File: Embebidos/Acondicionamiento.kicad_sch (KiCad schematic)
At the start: 20 parts, among them IC1 ESP32-WROVER-B__8MB_, SW1 SW_Reset, SW2 SW_Boot

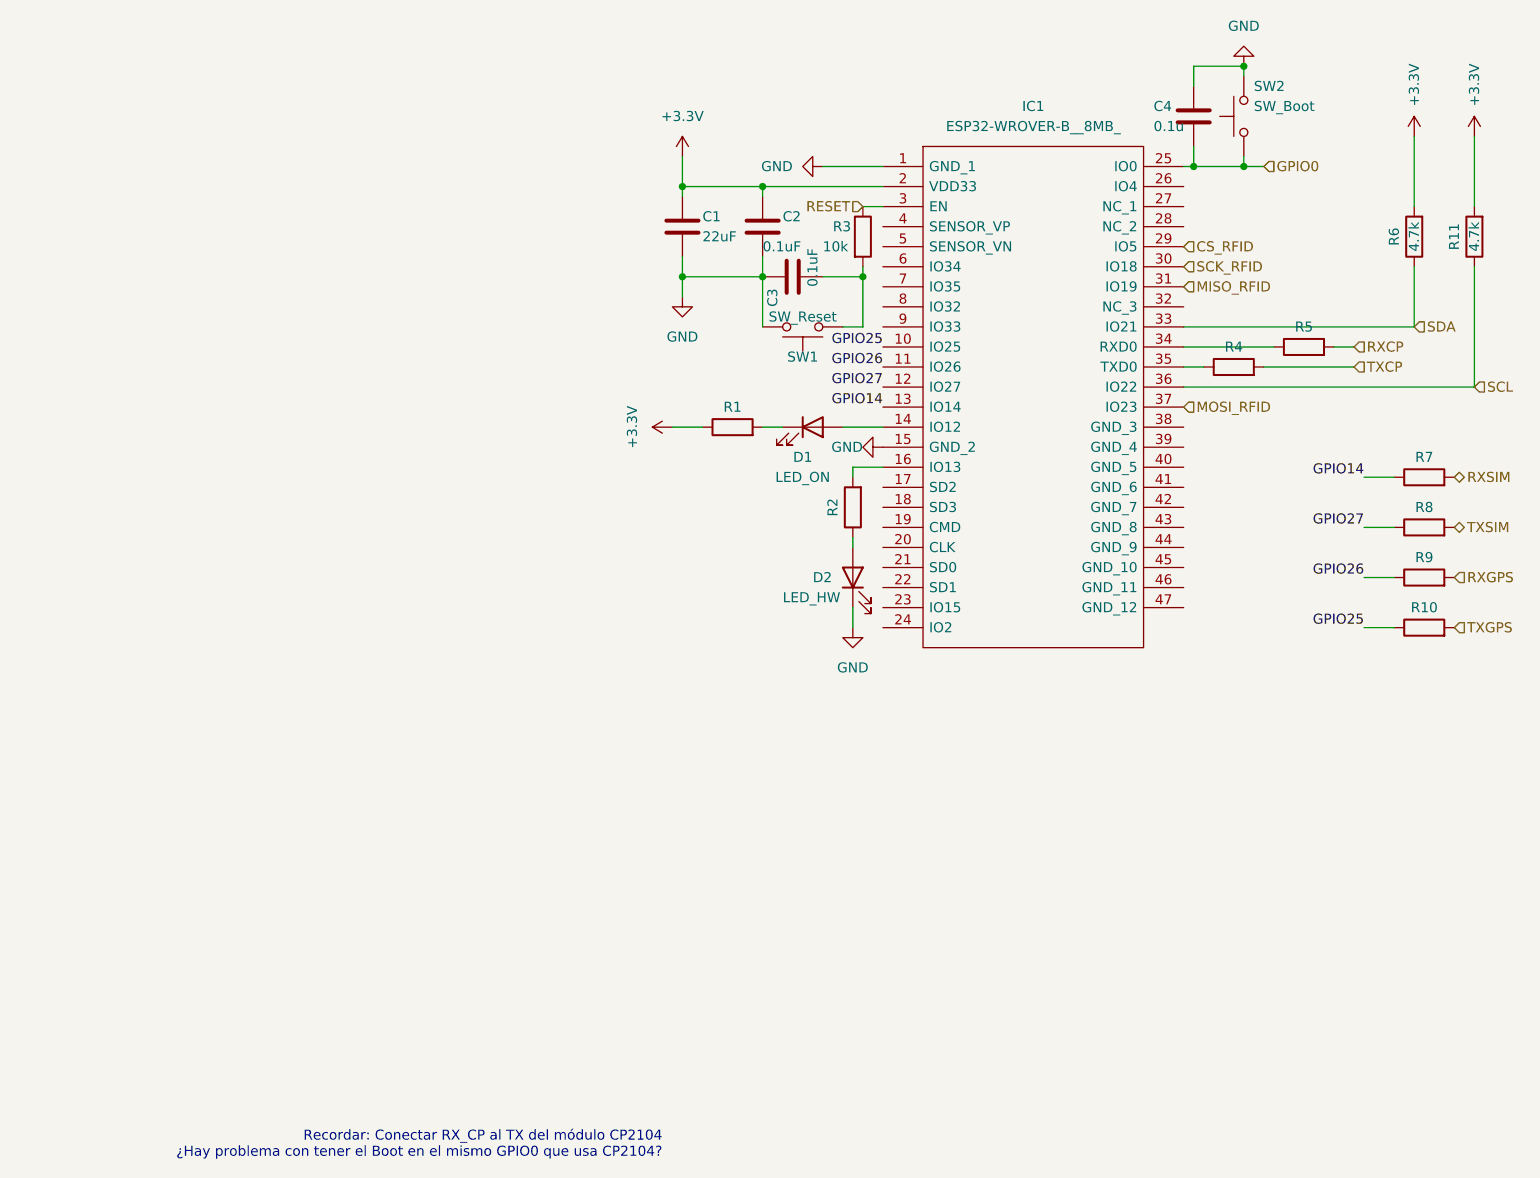
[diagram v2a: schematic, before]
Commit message: Luces delanteras, traseras, pantalla, e infrarrojo
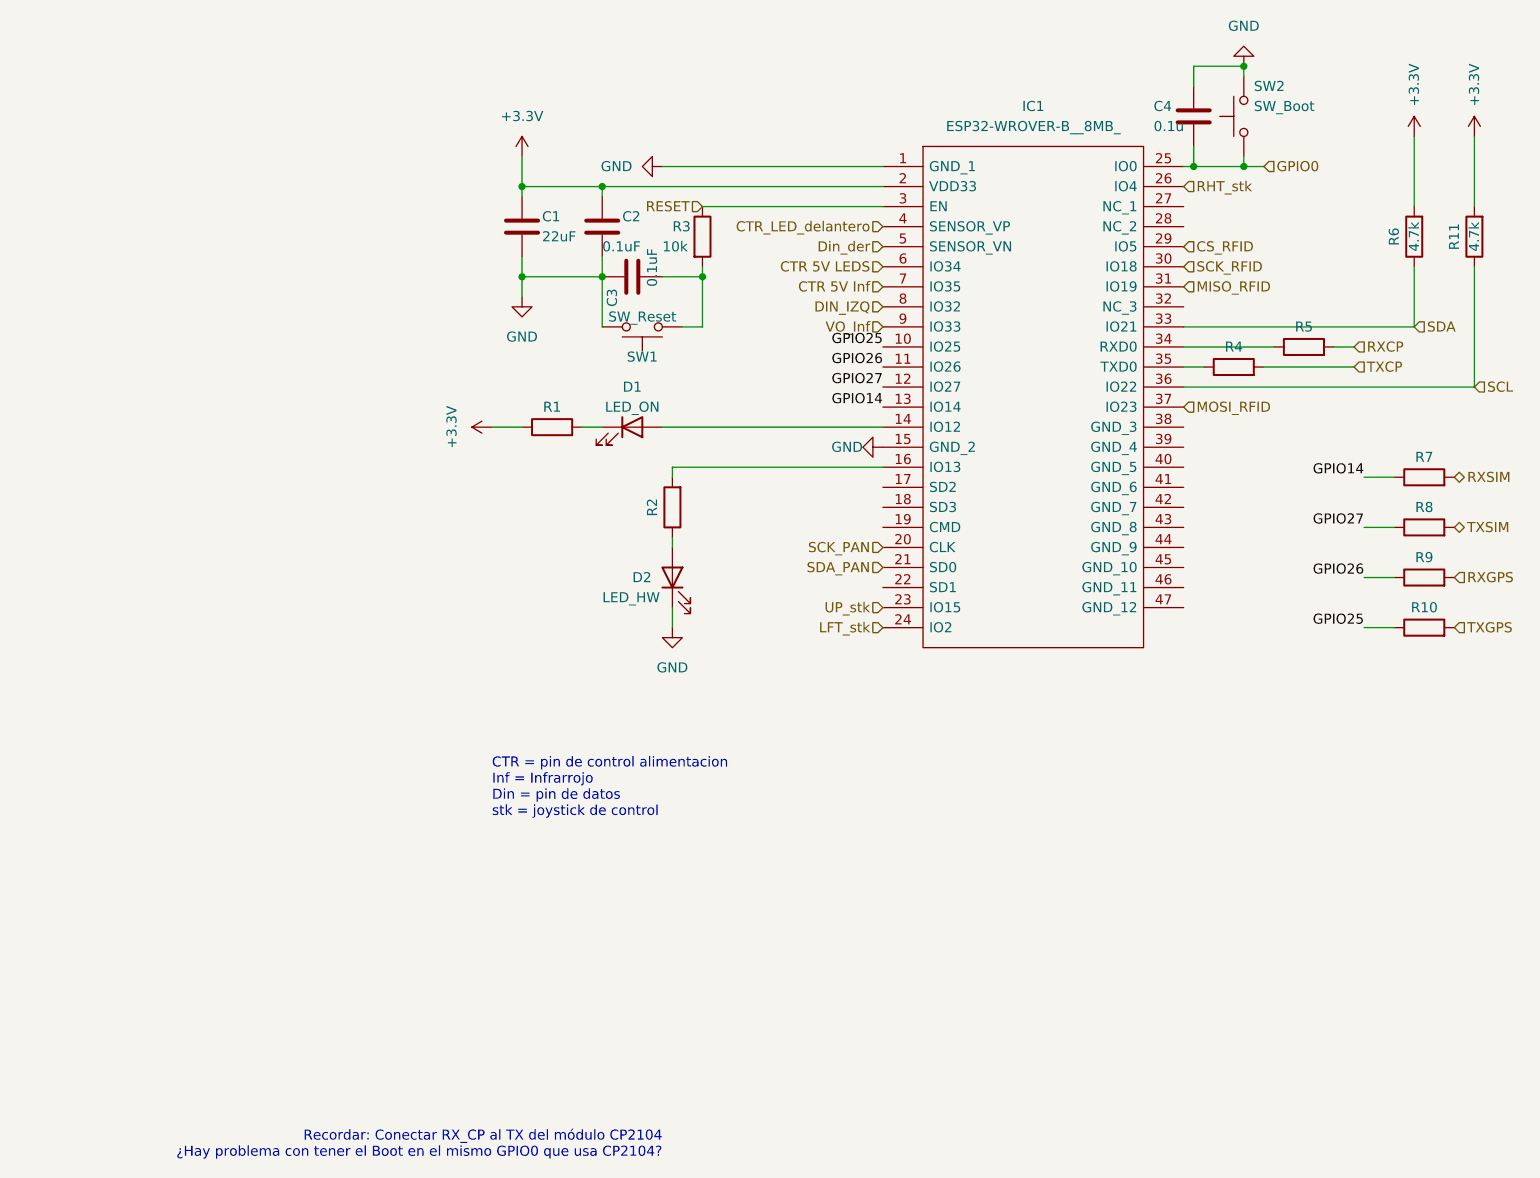
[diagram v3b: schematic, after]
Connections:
- net SCK_PAN: now reaches IC1.20 (CLK)
- net SDA_PAN: now reaches IC1.21 (SD0)
- net UP_stk: now reaches IC1.23 (IO15)
- net LFT_stk: now reaches IC1.24 (IO2)
- net RHT_stk: now reaches IC1.26 (IO4)
- net CTR_LED_delantero: now reaches IC1.4 (SENSOR_VP)
- net Din_der: now reaches IC1.5 (SENSOR_VN)
- net CTR 5V LEDS: now reaches IC1.6 (IO34)
- net CTR 5V Inf: now reaches IC1.7 (IO35)
- net DIN_IZQ: now reaches IC1.8 (IO32)
- net VO_Inf: now reaches IC1.9 (IO33)
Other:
- note added: "CTR = pin de control alimentacion Inf = Infrarrojo Din = pin de datos stk = joystick de control"
- moved on the sheet: C1, C2, C3, D1, D2, R1, R2, R3, SW1
